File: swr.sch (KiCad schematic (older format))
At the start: 12 parts

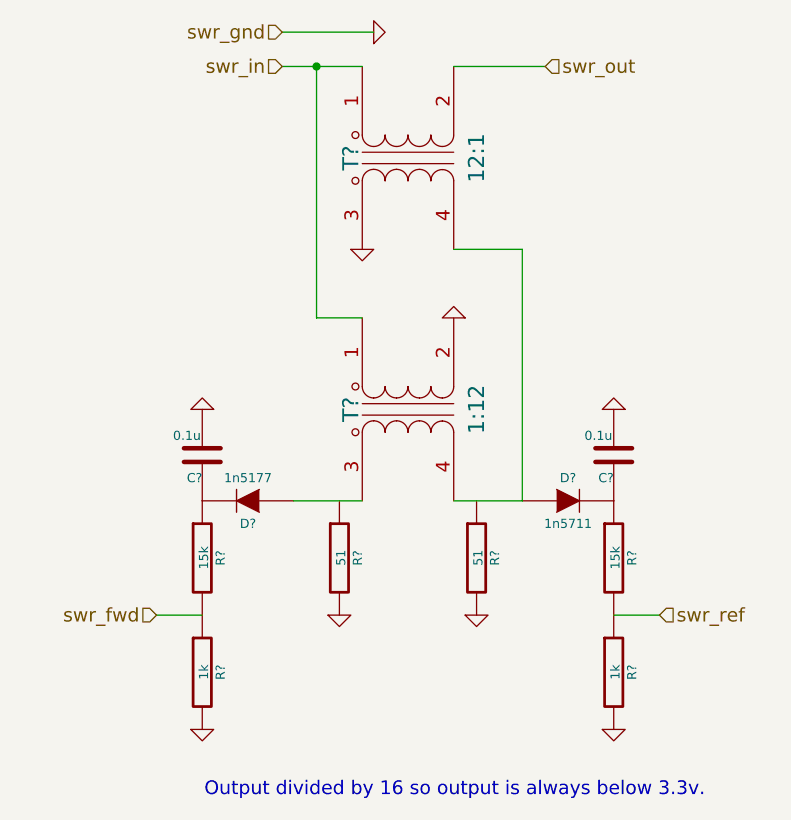
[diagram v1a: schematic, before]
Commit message: Annotated all schematics
- Added more caps to power supply
- Decided on power supply fuse part
- Changed 1n5711 SWR caps to BAT62
- Decided on MMBF170 for amp bias switch
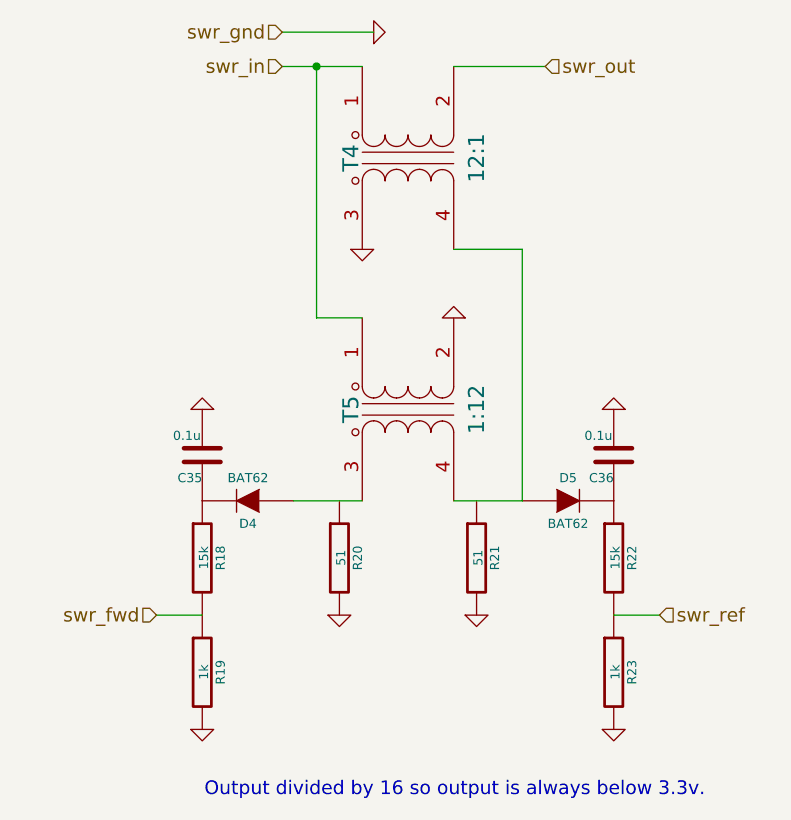
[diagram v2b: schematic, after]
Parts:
- D4: renamed from D?; value 1n5177 -> BAT62
- D5: renamed from D?; value 1n5711 -> BAT62
- gave numbers to parts that had none: 10
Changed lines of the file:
@@
 $Descr A4 11693 8268
 encoding utf-8
-Sheet 6 8
+Sheet 7 8
 Title "SWR Bridge"
 Date "22 Nov 2014"
@@
 $EndDescr
 $Comp
-L TRANSFO-dots T?
+L TRANSFO-dots T4
 U 1 1 547106DF
 P 5150 2950
-F 0 "T?" H 5150 3200 70  0000 C CNN
+F 0 "T4" H 5150 3200 70  0000 C CNN
 F 1 "12:1" H 5150 2650 70  0000 C CNN
 F 2 "" H 5150 2950 60  0000 C CNN
@@
 $EndComp
 $Comp
-L TRANSFO-dots T?
+L TRANSFO-dots T5
 U 1 1 547106F1
 P 5150 4050
-F 0 "T?" H 5150 4300 70  0000 C CNN
+F 0 "T5" H 5150 4300 70  0000 C CNN
 F 1 "1:12" H 5150 3750 70  0000 C CNN
 F 2 "" H 5150 4050 60  0000 C CNN
@@
 swr_in
 $Comp
-L GND #PWR?
+L GND #PWR91
 U 1 1 54710723
 P 5000 2400
-F 0 "#PWR?" H 5000 2400 30  0001 C CNN
+F 0 "#PWR91" H 5000 2400 30  0001 C CNN
 F 1 "GND" H 5000 2330 30  0001 C CNN
 F 2 "" H 5000 2400 60  0000 C CNN
@@
 swr_gnd
 $Comp
-L GND #PWR?
+L GND #PWR90
 U 1 1 5471074B
 P 4950 3350
-F 0 "#PWR?" H 4950 3350 30  0001 C CNN
+F 0 "#PWR90" H 4950 3350 30  0001 C CNN
 F 1 "GND" H 4950 3280 30  0001 C CNN
 F 2 "" H 4950 3350 60  0000 C CNN
@@
 $EndComp
 $Comp
-L GND #PWR?
+L GND #PWR92
 U 1 1 5471075F
 P 5350 3650
-F 0 "#PWR?" H 5350 3650 30  0001 C CNN
+F 0 "#PWR92" H 5350 3650 30  0001 C CNN
 F 1 "GND" H 5350 3580 30  0001 C CNN
 F 2 "" H 5350 3650 60  0000 C CNN
@@
 	4650 4450 4950 4450
 $Comp
-L R R?
+L R R20
 U 1 1 54710792
 P 4850 4700
-F 0 "R?" V 4930 4700 40  0000 C CNN
+F 0 "R20" V 4930 4700 40  0000 C CNN
 F 1 "51" V 4857 4701 40  0000 C CNN
 F 2 "" V 4780 4700 30  0000 C CNN
@@
 $EndComp
 $Comp
-L R R?
+L R R21
 U 1 1 547107A4
 P 5450 4700
-F 0 "R?" V 5530 4700 40  0000 C CNN
+F 0 "R21" V 5530 4700 40  0000 C CNN
 F 1 "51" V 5457 4701 40  0000 C CNN
 F 2 "" V 5380 4700 30  0000 C CNN
@@
 $EndComp
 $Comp
-L DIODE D?
+L DIODE D5
 U 1 1 547107BB
 P 5850 4450
-F 0 "D?" H 5850 4550 40  0000 C CNN
-F 1 "1n5711" H 5850 4350 40  0000 C CNN
+F 0 "D5" H 5850 4550 40  0000 C CNN
+F 1 "BAT62" H 5850 4350 40  0000 C CNN
 F 2 "" H 5850 4450 60  0000 C CNN
 F 3 "" H 5850 4450 60  0000 C CNN
@@
 $EndComp
 $Comp
-L DIODE D?
+L DIODE D4
 U 1 1 547107CD
 P 4450 4450
-F 0 "D?" H 4450 4550 40  0000 C CNN
-F 1 "1n5177" H 4450 4350 40  0000 C CNN
+F 0 "D4" H 4450 4550 40  0000 C CNN
+F 1 "BAT62" H 4450 4350 40  0000 C CNN
 F 2 "" H 4450 4450 60  0000 C CNN
 F 3 "" H 4450 4450 60  0000 C CNN
@@
 $EndComp
 $Comp
-L GND #PWR?
+L GND #PWR89
 U 1 1 54710804
 P 4850 4950
-F 0 "#PWR?" H 4850 4950 30  0001 C CNN
+F 0 "#PWR89" H 4850 4950 30  0001 C CNN
 F 1 "GND" H 4850 4880 30  0001 C CNN
 F 2 "" H 4850 4950 60  0000 C CNN
@@
 $EndComp
 $Comp
-L GND #PWR?
+L GND #PWR93
 U 1 1 54710818
 P 5450 4950
-F 0 "#PWR?" H 5450 4950 30  0001 C CNN
+F 0 "#PWR93" H 5450 4950 30  0001 C CNN
 F 1 "GND" H 5450 4880 30  0001 C CNN
 F 2 "" H 5450 4950 60  0000 C CNN
@@
 $EndComp
 $Comp
-L C C?
+L C C36
 U 1 1 5471082C
 P 6050 4250
-F 0 "C?" H 6050 4350 40  0000 L CNN
+F 0 "C36" H 6050 4350 40  0000 L CNN
 F 1 "0.1u" H 6056 4165 40  0000 L CNN
 F 2 "" H 6088 4100 30  0000 C CNN
@@
 $EndComp
 $Comp
-L C C?
+L C C35
 U 1 1 5471083E
 P 4250 4250
-F 0 "C?" H 4250 4350 40  0000 L CNN
+F 0 "C35" H 4250 4350 40  0000 L CNN
 F 1 "0.1u" H 4256 4165 40  0000 L CNN
 F 2 "" H 4288 4100 30  0000 C CNN
@@
 $EndComp
 $Comp
-L GND #PWR?
+L GND #PWR87
 U 1 1 5471084B
 P 4250 4050
-F 0 "#PWR?" H 4250 4050 30  0001 C CNN
+F 0 "#PWR87" H 4250 4050 30  0001 C CNN
 F 1 "GND" H 4250 3980 30  0001 C CNN
 F 2 "" H 4250 4050 60  0000 C CNN
@@
 $EndComp
 $Comp
-L GND #PWR?
+L GND #PWR94
 U 1 1 54710867
 P 6050 4050
-F 0 "#PWR?" H 6050 4050 30  0001 C CNN
+F 0 "#PWR94" H 6050 4050 30  0001 C CNN
 F 1 "GND" H 6050 3980 30  0001 C CNN
 F 2 "" H 6050 4050 60  0000 C CNN
@@
 $EndComp
 $Comp
-L R R?
+L R R22
 U 1 1 5471087E
 P 6050 4700
-F 0 "R?" V 6130 4700 40  0000 C CNN
+F 0 "R22" V 6130 4700 40  0000 C CNN
 F 1 "15k" V 6057 4701 40  0000 C CNN
 F 2 "" V 5980 4700 30  0000 C CNN
@@
 $EndComp
 $Comp
-L R R?
+L R R23
 U 1 1 54710890
 P 6050 5200
-F 0 "R?" V 6130 5200 40  0000 C CNN
+F 0 "R23" V 6130 5200 40  0000 C CNN
 F 1 "1k" V 6057 5201 40  0000 C CNN
 F 2 "" V 5980 5200 30  0000 C CNN
@@
 $EndComp
 $Comp
-L R R?
+L R R18
 U 1 1 5471089B
 P 4250 4700
-F 0 "R?" V 4330 4700 40  0000 C CNN
+F 0 "R18" V 4330 4700 40  0000 C CNN
 F 1 "15k" V 4257 4701 40  0000 C CNN
 F 2 "" V 4180 4700 30  0000 C CNN
@@
 $EndComp
 $Comp
-L R R?
+L R R19
 U 1 1 547108A6
 P 4250 5200
-F 0 "R?" V 4330 5200 40  0000 C CNN
+F 0 "R19" V 4330 5200 40  0000 C CNN
 F 1 "1k" V 4257 5201 40  0000 C CNN
 F 2 "" V 4180 5200 30  0000 C CNN
@@
 $EndComp
 $Comp
-L GND #PWR?
+L GND #PWR88
 U 1 1 547108D1
 P 4250 5450
-F 0 "#PWR?" H 4250 5450 30  0001 C CNN
+F 0 "#PWR88" H 4250 5450 30  0001 C CNN
 F 1 "GND" H 4250 5380 30  0001 C CNN
 F 2 "" H 4250 5450 60  0000 C CNN
@@
 $EndComp
 $Comp
-L GND #PWR?
+L GND #PWR95
 U 1 1 547108E5
 P 6050 5450
-F 0 "#PWR?" H 6050 5450 30  0001 C CNN
+F 0 "#PWR95" H 6050 5450 30  0001 C CNN
 F 1 "GND" H 6050 5380 30  0001 C CNN
 F 2 "" H 6050 5450 60  0000 C CNN

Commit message: Associate more footprints
- Removed flyback diodes from amp
- Changed BAT62 -> SD101 (BAT62 is EOL)
- Changed R and C footprints for hand-soldered versions
- Associated through-hole cap footprints
- Associated regulator footprints
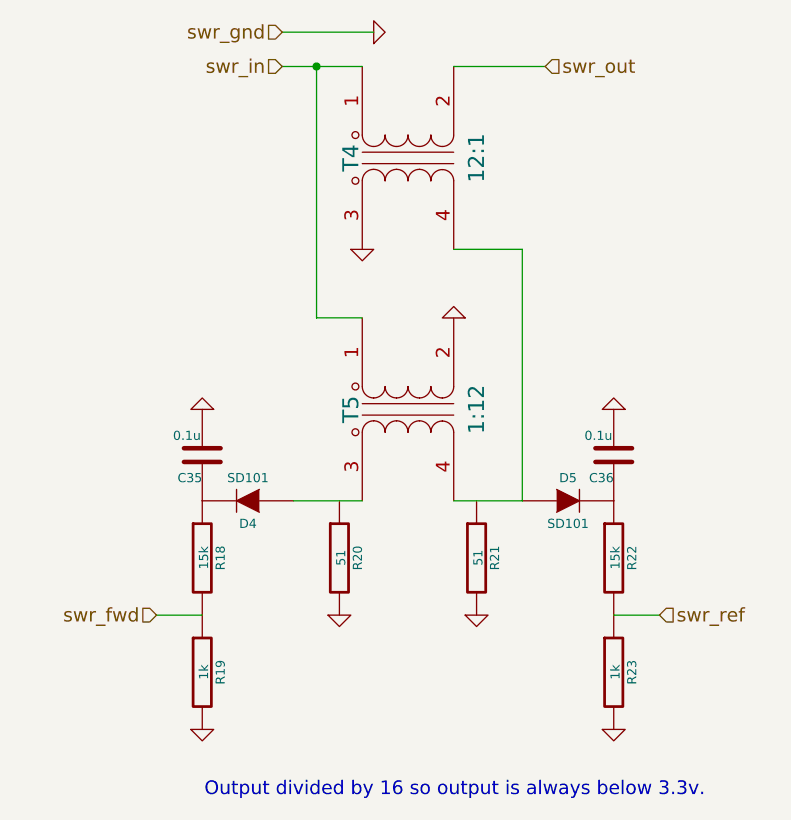
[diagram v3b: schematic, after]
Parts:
- C35, C36: footprint (none) -> Capacitors_SMD:C_0805_HandSoldering
- D4, D5: value BAT62 -> SD101
- R18, R19, R20, R21, R22, R23: footprint (none) -> Resistors_SMD:R_1206_HandSoldering
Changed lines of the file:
@@
 LIBS:transformers
 LIBS:qrpamp-cache
-EELAYER 24 0
+EELAYER 25 0
 EELAYER END
 $Descr A4 11693 8268
@@
 F 0 "T4" H 5150 3200 70  0000 C CNN
 F 1 "12:1" H 5150 2650 70  0000 C CNN
-F 2 "" H 5150 2950 60  0000 C CNN
+F 2 "" H 5150 2950 60  0001 C CNN
 F 3 "" H 5150 2950 60  0000 C CNN
 	1    5150 2950
@@
 F 0 "T5" H 5150 4300 70  0000 C CNN
 F 1 "1:12" H 5150 3750 70  0000 C CNN
-F 2 "" H 5150 4050 60  0000 C CNN
+F 2 "" H 5150 4050 60  0001 C CNN
 F 3 "" H 5150 4050 60  0000 C CNN
 	1    5150 4050
@@
 F 0 "R20" V 4930 4700 40  0000 C CNN
 F 1 "51" V 4857 4701 40  0000 C CNN
-F 2 "" V 4780 4700 30  0000 C CNN
+F 2 "Resistors_SMD:R_1206_HandSoldering" V 4780 4700 30  0001 C CNN
 F 3 "" H 4850 4700 30  0000 C CNN
 	1    4850 4700
@@
 F 0 "R21" V 5530 4700 40  0000 C CNN
 F 1 "51" V 5457 4701 40  0000 C CNN
-F 2 "" V 5380 4700 30  0000 C CNN
+F 2 "Resistors_SMD:R_1206_HandSoldering" V 5380 4700 30  0001 C CNN
 F 3 "" H 5450 4700 30  0000 C CNN
 	1    5450 4700
@@
 P 5850 4450
 F 0 "D5" H 5850 4550 40  0000 C CNN
-F 1 "BAT62" H 5850 4350 40  0000 C CNN
-F 2 "" H 5850 4450 60  0000 C CNN
+F 1 "SD101" H 5850 4350 40  0000 C CNN
+F 2 "" H 5850 4450 60  0001 C CNN
 F 3 "" H 5850 4450 60  0000 C CNN
 	1    5850 4450
@@
 P 4450 4450
 F 0 "D4" H 4450 4550 40  0000 C CNN
-F 1 "BAT62" H 4450 4350 40  0000 C CNN
-F 2 "" H 4450 4450 60  0000 C CNN
+F 1 "SD101" H 4450 4350 40  0000 C CNN
+F 2 "" H 4450 4450 60  0001 C CNN
 F 3 "" H 4450 4450 60  0000 C CNN
 	1    4450 4450
@@
 F 0 "C36" H 6050 4350 40  0000 L CNN
 F 1 "0.1u" H 6056 4165 40  0000 L CNN
-F 2 "" H 6088 4100 30  0000 C CNN
+F 2 "Capacitors_SMD:C_0805_HandSoldering" H 6088 4100 30  0001 C CNN
 F 3 "" H 6050 4250 60  0000 C CNN
 	1    6050 4250
@@
 F 0 "C35" H 4250 4350 40  0000 L CNN
 F 1 "0.1u" H 4256 4165 40  0000 L CNN
-F 2 "" H 4288 4100 30  0000 C CNN
+F 2 "Capacitors_SMD:C_0805_HandSoldering" H 4288 4100 30  0001 C CNN
 F 3 "" H 4250 4250 60  0000 C CNN
 	1    4250 4250
@@
 F 0 "R22" V 6130 4700 40  0000 C CNN
 F 1 "15k" V 6057 4701 40  0000 C CNN
-F 2 "" V 5980 4700 30  0000 C CNN
+F 2 "Resistors_SMD:R_1206_HandSoldering" V 5980 4700 30  0001 C CNN
 F 3 "" H 6050 4700 30  0000 C CNN
 	1    6050 4700
@@
 F 0 "R23" V 6130 5200 40  0000 C CNN
 F 1 "1k" V 6057 5201 40  0000 C CNN
-F 2 "" V 5980 5200 30  0000 C CNN
+F 2 "Resistors_SMD:R_1206_HandSoldering" V 5980 5200 30  0001 C CNN
 F 3 "" H 6050 5200 30  0000 C CNN
 	1    6050 5200
@@
 F 0 "R18" V 4330 4700 40  0000 C CNN
 F 1 "15k" V 4257 4701 40  0000 C CNN
-F 2 "" V 4180 4700 30  0000 C CNN
+F 2 "Resistors_SMD:R_1206_HandSoldering" V 4180 4700 30  0001 C CNN
 F 3 "" H 4250 4700 30  0000 C CNN
 	1    4250 4700
@@
 F 0 "R19" V 4330 5200 40  0000 C CNN
 F 1 "1k" V 4257 5201 40  0000 C CNN
-F 2 "" V 4180 5200 30  0000 C CNN
+F 2 "Resistors_SMD:R_1206_HandSoldering" V 4180 5200 30  0001 C CNN
 F 3 "" H 4250 5200 30  0000 C CNN
 	1    4250 5200

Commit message: Finished band filters schematic
- Associated last of the capacitors with footprints
- Associated inductors
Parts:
- D4, D5: footprint (none) -> nu9j-footprints:SOD-123
- T4, T5: footprint (none) -> nu9j-footprints:TOROID-50
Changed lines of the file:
@@
 F 0 "T4" H 5150 3200 70  0000 C CNN
 F 1 "12:1" H 5150 2650 70  0000 C CNN
-F 2 "" H 5150 2950 60  0001 C CNN
+F 2 "nu9j-footprints:TOROID-50" H 5150 2950 60  0001 C CNN
 F 3 "" H 5150 2950 60  0000 C CNN
 	1    5150 2950
@@
 F 0 "T5" H 5150 4300 70  0000 C CNN
 F 1 "1:12" H 5150 3750 70  0000 C CNN
-F 2 "" H 5150 4050 60  0001 C CNN
+F 2 "nu9j-footprints:TOROID-50" H 5150 4050 60  0001 C CNN
 F 3 "" H 5150 4050 60  0000 C CNN
 	1    5150 4050
@@
 swr_in
 $Comp
-L GND #PWR91
+L GND #PWR087
 U 1 1 54710723
 P 5000 2400
-F 0 "#PWR91" H 5000 2400 30  0001 C CNN
+F 0 "#PWR087" H 5000 2400 30  0001 C CNN
 F 1 "GND" H 5000 2330 30  0001 C CNN
 F 2 "" H 5000 2400 60  0000 C CNN
@@
 swr_gnd
 $Comp
-L GND #PWR90
+L GND #PWR088
 U 1 1 5471074B
 P 4950 3350
-F 0 "#PWR90" H 4950 3350 30  0001 C CNN
+F 0 "#PWR088" H 4950 3350 30  0001 C CNN
 F 1 "GND" H 4950 3280 30  0001 C CNN
 F 2 "" H 4950 3350 60  0000 C CNN
@@
 $EndComp
 $Comp
-L GND #PWR92
+L GND #PWR089
 U 1 1 5471075F
 P 5350 3650
-F 0 "#PWR92" H 5350 3650 30  0001 C CNN
+F 0 "#PWR089" H 5350 3650 30  0001 C CNN
 F 1 "GND" H 5350 3580 30  0001 C CNN
 F 2 "" H 5350 3650 60  0000 C CNN
@@
 F 0 "D5" H 5850 4550 40  0000 C CNN
 F 1 "SD101" H 5850 4350 40  0000 C CNN
-F 2 "" H 5850 4450 60  0001 C CNN
+F 2 "nu9j-footprints:SOD-123" H 5850 4450 60  0001 C CNN
 F 3 "" H 5850 4450 60  0000 C CNN
 	1    5850 4450
@@
 F 0 "D4" H 4450 4550 40  0000 C CNN
 F 1 "SD101" H 4450 4350 40  0000 C CNN
-F 2 "" H 4450 4450 60  0001 C CNN
+F 2 "nu9j-footprints:SOD-123" H 4450 4450 60  0001 C CNN
 F 3 "" H 4450 4450 60  0000 C CNN
 	1    4450 4450
@@
 $EndComp
 $Comp
-L GND #PWR89
+L GND #PWR090
 U 1 1 54710804
 P 4850 4950
-F 0 "#PWR89" H 4850 4950 30  0001 C CNN
+F 0 "#PWR090" H 4850 4950 30  0001 C CNN
 F 1 "GND" H 4850 4880 30  0001 C CNN
 F 2 "" H 4850 4950 60  0000 C CNN
@@
 $EndComp
 $Comp
-L GND #PWR93
+L GND #PWR091
 U 1 1 54710818
 P 5450 4950
-F 0 "#PWR93" H 5450 4950 30  0001 C CNN
+F 0 "#PWR091" H 5450 4950 30  0001 C CNN
 F 1 "GND" H 5450 4880 30  0001 C CNN
 F 2 "" H 5450 4950 60  0000 C CNN
@@
 $EndComp
 $Comp
-L GND #PWR87
+L GND #PWR092
 U 1 1 5471084B
 P 4250 4050
-F 0 "#PWR87" H 4250 4050 30  0001 C CNN
+F 0 "#PWR092" H 4250 4050 30  0001 C CNN
 F 1 "GND" H 4250 3980 30  0001 C CNN
 F 2 "" H 4250 4050 60  0000 C CNN
@@
 $EndComp
 $Comp
-L GND #PWR94
+L GND #PWR093
 U 1 1 54710867
 P 6050 4050
-F 0 "#PWR94" H 6050 4050 30  0001 C CNN
+F 0 "#PWR093" H 6050 4050 30  0001 C CNN
 F 1 "GND" H 6050 3980 30  0001 C CNN
 F 2 "" H 6050 4050 60  0000 C CNN
@@
 $EndComp
 $Comp
-L GND #PWR88
+L GND #PWR094
 U 1 1 547108D1
 P 4250 5450
-F 0 "#PWR88" H 4250 5450 30  0001 C CNN
+F 0 "#PWR094" H 4250 5450 30  0001 C CNN
 F 1 "GND" H 4250 5380 30  0001 C CNN
 F 2 "" H 4250 5450 60  0000 C CNN
@@
 $EndComp
 $Comp
-L GND #PWR95
+L GND #PWR095
 U 1 1 547108E5
 P 6050 5450
-F 0 "#PWR95" H 6050 5450 30  0001 C CNN
+F 0 "#PWR095" H 6050 5450 30  0001 C CNN
 F 1 "GND" H 6050 5380 30  0001 C CNN
 F 2 "" H 6050 5450 60  0000 C CNN

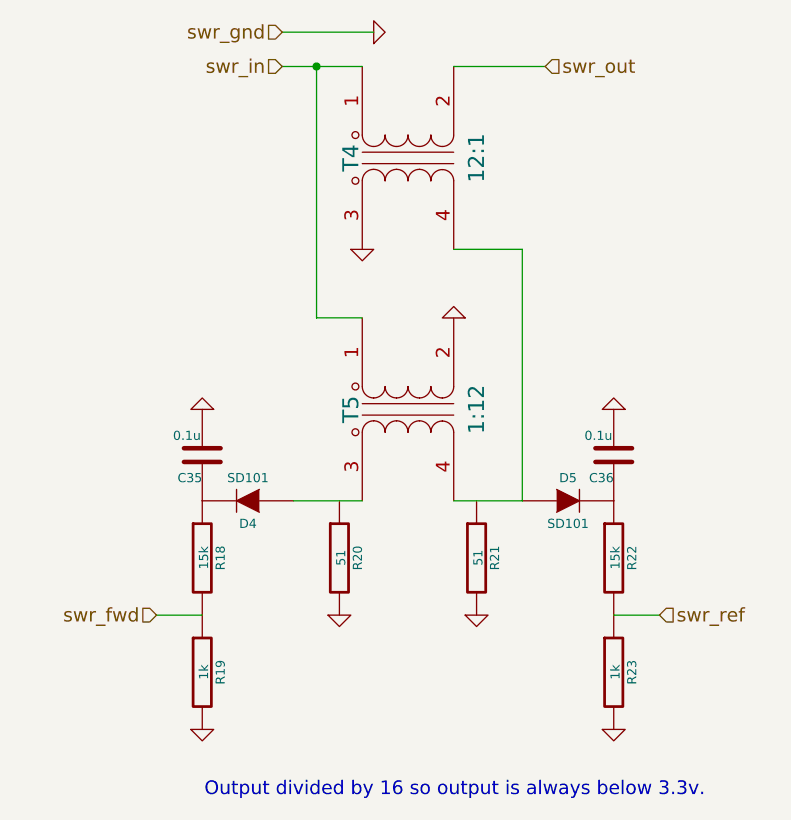
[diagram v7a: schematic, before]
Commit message: Fixed pin assignment issues in pcb layout
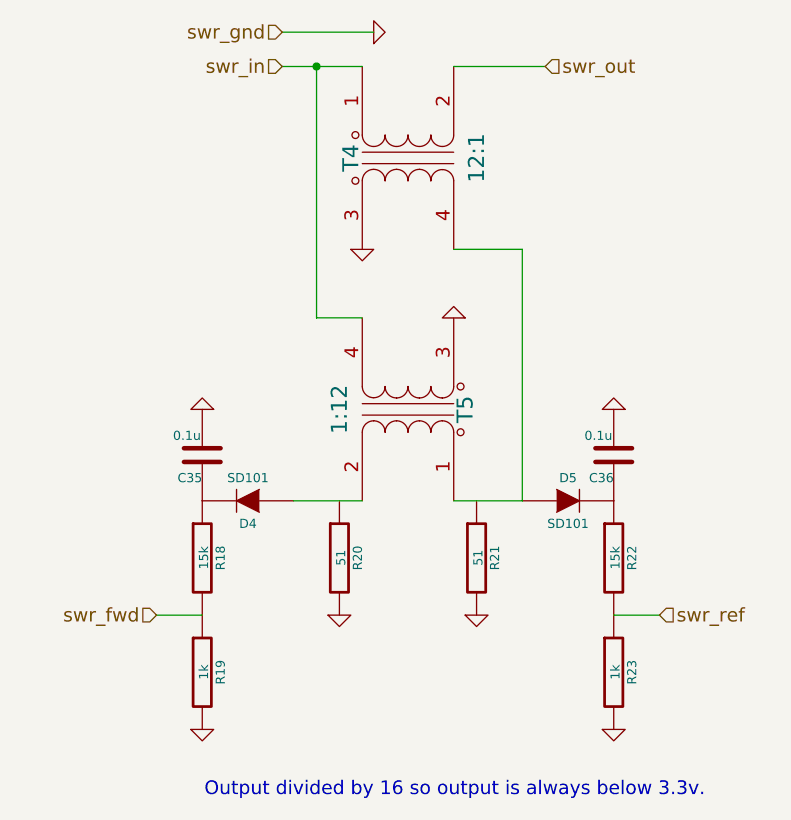
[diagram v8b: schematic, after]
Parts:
- T4, T5: footprint nu9j-footprints:TOROID-50 -> nu9j-footprints:TOROID2-50-singleturn
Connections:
- net GND: now also T5.3 (SA); no longer T5.2 (PB)
- net swr_in: now also T5.4 (SB); no longer T5.1 (PA)
- net at D5.1 (A), T4.4 (SB): now also T5.1 (PA); no longer T5.4 (SB)
- net at D4.1 (A): now also T5.2 (PB); no longer T5.3 (SA)
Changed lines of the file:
@@
 F 0 "T4" H 5150 3200 70  0000 C CNN
 F 1 "12:1" H 5150 2650 70  0000 C CNN
-F 2 "nu9j-footprints:TOROID-50" H 5150 2950 60  0001 C CNN
+F 2 "nu9j-footprints:TOROID2-50-singleturn" H 5150 2950 60  0001 C CNN
 F 3 "" H 5150 2950 60  0000 C CNN
 	1    5150 2950
@@
 F 0 "T5" H 5150 4300 70  0000 C CNN
 F 1 "1:12" H 5150 3750 70  0000 C CNN
-F 2 "nu9j-footprints:TOROID-50" H 5150 4050 60  0001 C CNN
+F 2 "nu9j-footprints:TOROID2-50-singleturn" H 5150 4050 60  0001 C CNN
 F 3 "" H 5150 4050 60  0000 C CNN
 	1    5150 4050
-	0    -1   1    0
+	0    1    -1   0
 $EndComp
 Wire Wire Line
